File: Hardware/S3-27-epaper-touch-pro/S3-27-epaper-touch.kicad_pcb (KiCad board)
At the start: 2 copper layers, 65.4 x 71 mm, 102 parts, among them J1 AFC24-S24FIC-00, J10 Conn_01x06_Pin, J2 Conn_01x06, J3 Conn_01x06, J4 Conn_01x06_Female, J5 Groove sensor, J6 Conn_01x05_Pin, J7 Conn_01x04_Pin, J8 Conn_01x06, Q1 Si1308, Q2 Si2301, SW1 SW_Push, SW2 SW_Push, SW3 SW_Push, SW4 SW_Push, SW5 SW_Push, SW6 SW_Push, SW7 SW_Push, SW8 SW_Push, SW9 SW_Push, U1 ESP32-S3-WROOM-1-N8, U2 RT9013, U3 KoreanHropartsElecTYPE-C-31-M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, U5 BME680, U6 TPL5110, U7 RFM95W-868S2, U8 LSM6DSL

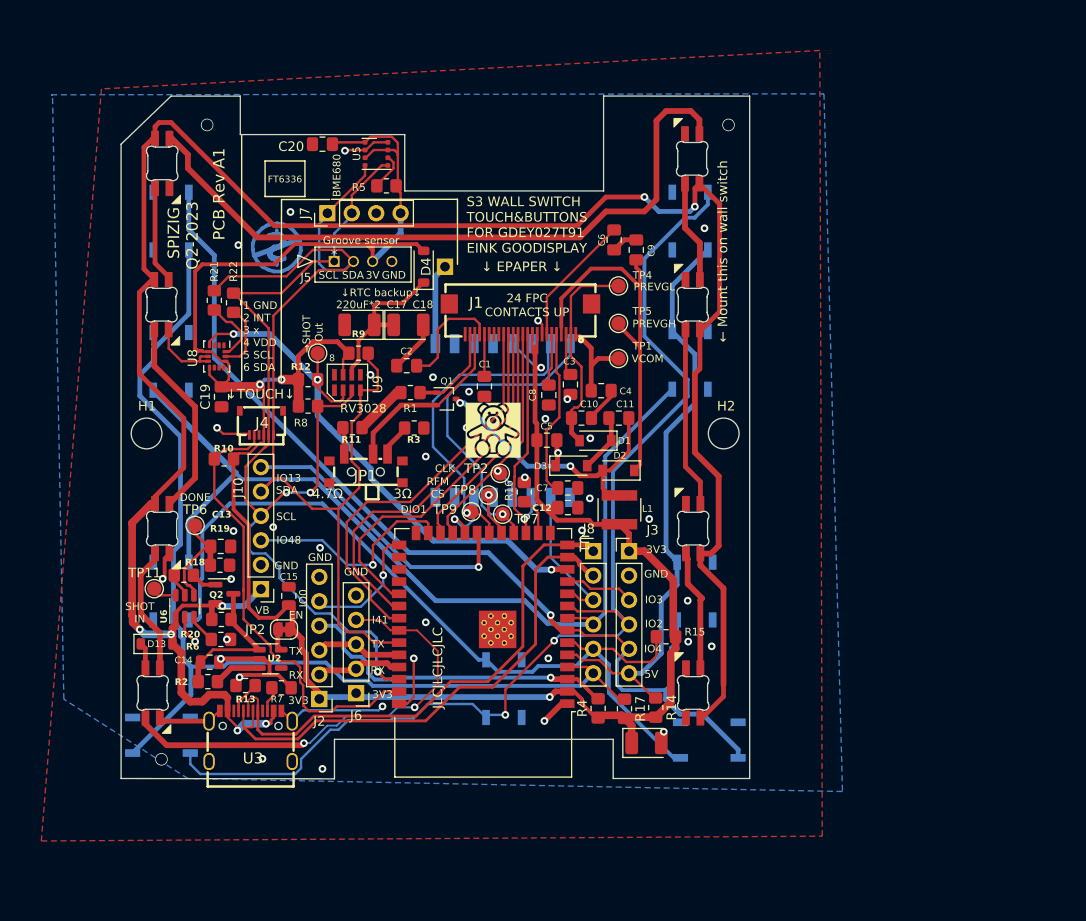
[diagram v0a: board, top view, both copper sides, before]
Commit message: Changed Footprint of BME680 and Silkscreen
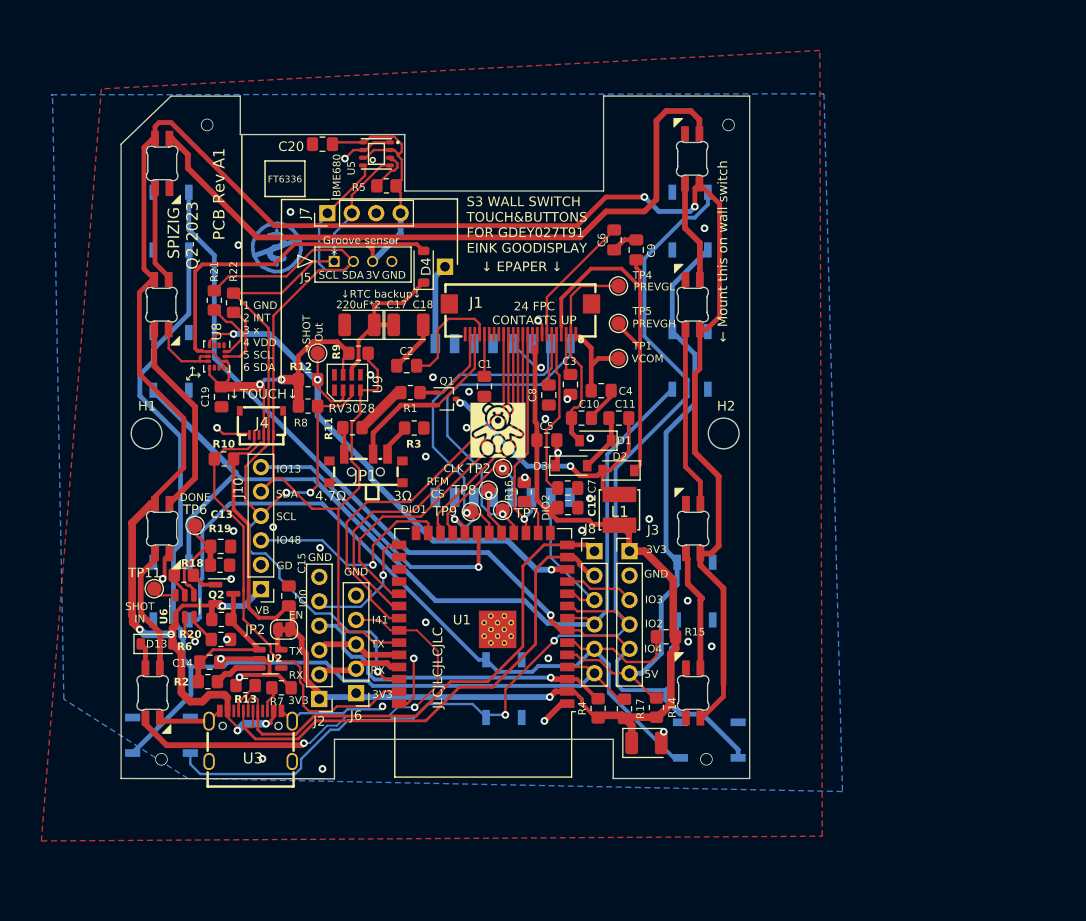
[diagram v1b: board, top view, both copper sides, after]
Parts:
- C14, C15: footprint Capacitor_SMD:C_0805_2012Metric -> Capacitor_SMD:C_0805_2012Metric_Pad1.18x1.45mm_HandSolder
- J4: value Conn_01x06_Female -> TochConn
- L1: footprint footprint:SWPA4030S1R0NT -> tp4056:IND-SMD_L4.0-W4.0
- R10, R14, R15, R17, R8, R9: value 4.7K -> 10k
- R16: value 0R -> N.C.
- R2: value 5k11 -> 10k
- R5: value 4.7K -> 10K
- U5: footprint Package_LGA:Bosch_LGA-8_3x3mm_P0.8mm_ClockwisePinNumbering -> tp4056:LGA-8_L3.0-W3.0-P0.80-TR
- moved H4 2.85 mm to (142.0, 105.0)
- moved TP2 0.56 mm to (144.5, 93.8)
- moved H3 0.50 mm to (144.0, 89.8)
- moved TP8 0.50 mm to (143.0, 96.0)
- moved TP7 0.40 mm to (144.5, 98.1)
- moved J8 0.12 mm to (154.1, 102.3)
- moved R14 0.07 mm to (160.5, 118.6)
- turned U5 to 0 degrees
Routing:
- net +3V3: track 233.0 -> 233.9 mm
- net Net-(U5-SDI): track 3.97 -> 4.67 mm
- net (no net): vias 3 -> 4
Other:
- board text added: "DIO2"
- board text added: "E-Paper&LoRa Pins: ■ EPD CS GPIO47 ■ EPD CLK GPIO21 ■ EPD BSY GPIO40 ■ EPD RST GPIO39 ■ EPD DC GPIO38 ■ EPD MOSI GPIO09"
- board text added: "GD"
- board text added: "↓"
- board text added: "■ I²C SDA IO42 ■ I²C SCL IO02 ■ TCH INT IO01 ■ SK6812 IO41 ■ Relay ON IO48 ■ Relay OFF IO13"
- board text removed: "8"
- board text removed: "E-Paper&Lora Pins: ■ EPD CS GPIO47 ■ EPD CLK GPIO21 ■ EPD BUSY GPIO40 ■ EPD RST GPIO39 ■ EPD DC GPIO38 ■ EPD MOSI GPIO09"
- board text removed: "■ I²C SDA GPIO47 ■ I²C SCL GPIO40 ■ TCH INT GPIO39 ■ SK6812 GPIO38 ■ Relay ON 48 ■ Relay OFF 13"

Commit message: Found a wiring Bug on the BME680
SDA had no pinning
wired several other lines with bigger lines
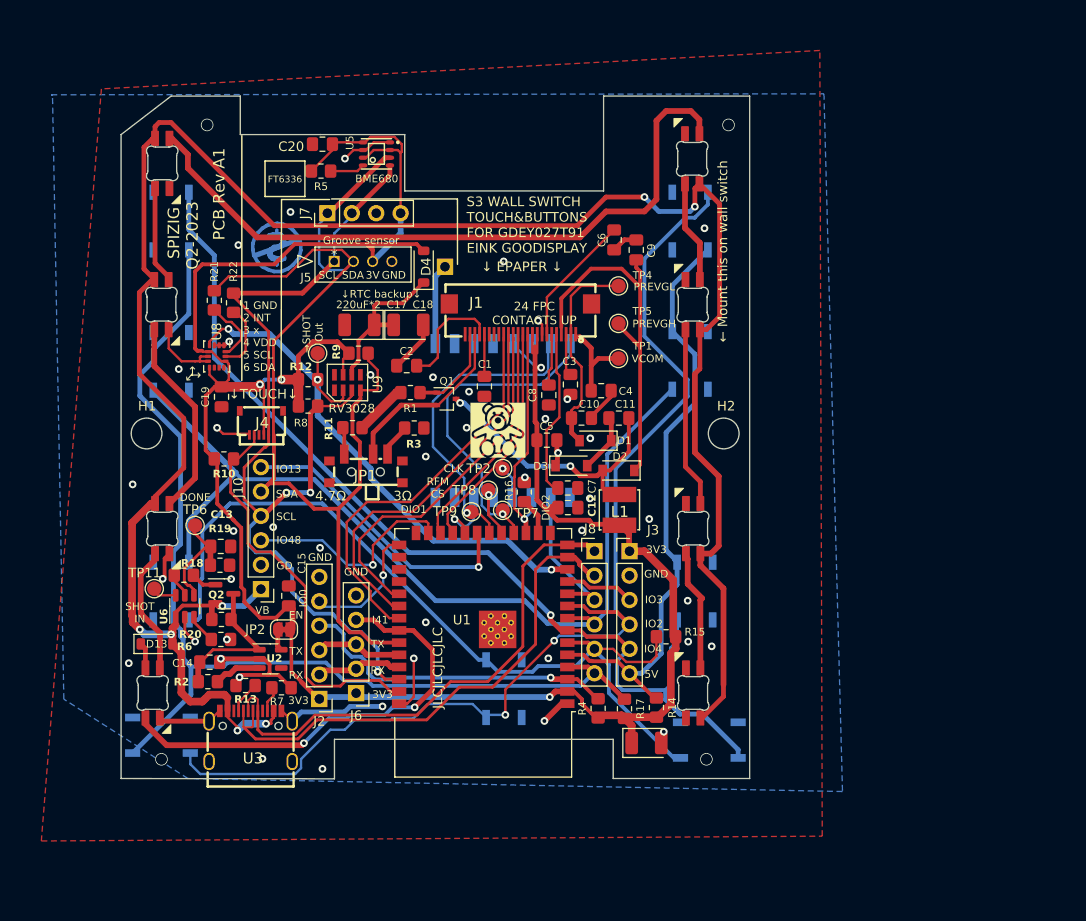
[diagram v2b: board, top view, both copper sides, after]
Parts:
- R10, R14, R15, R17, R2, R8, R9: value 10k -> 10K
- R12, R18, R19, R4, R6: value 10 K -> 10K
- R20: value 10 K -> N.C.
- moved R5 6.98 mm to (125.6, 62.8), turned to 180 degrees
- turned R10 to 0 degrees
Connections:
- R5 pad 1: Net-(U5-SDI) -> Net-(U5-SDO)
- U5 pad 3: Net-(U5-SDI) -> /TOUCH_SDA
- U5 pad 5: /TOUCH_SDA -> Net-(U5-SDO)
- U8 pad 1: unconnected-(U8-SDO/SA0-Pad1) -> GND
- U8 pad 2: unconnected-(U8-SDX-Pad2) -> GND
- U8 pad 3: unconnected-(U8-SCX-Pad3) -> GND
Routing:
- net +3V3: track 233.9 -> 242.3 mm
- net /ROW1: track 103.7 -> 111.0 mm
- net /TOUCH_SDA: track 111.7 -> 118.1 mm
- net /TOUCH_INT: track 47.5 -> 41.4 mm
- net Net-(U5-SDI): track 4.67 -> 0.00 mm
- net Net-(U5-SDO): track 0.00 -> 3.61 mm
- net /IO_15: track 98.7 -> 101.8 mm
- net GND: track 83.6 -> 85.8 mm, vias 39 -> 44
- net /IO_16: track 117.8 -> 119.6 mm
- net /EPD_MOSI: track 24.3 -> 25.9 mm
- net /IO_18: track 7.34 -> 8.75 mm
- net /SK6812_DATA: track 47.9 -> 47.2 mm
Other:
- outline, holes or cut-outs redrawn
- board text added: "@USPIZIG Q2/2023"
- board text removed: "@SPIZIG Q2/2023"

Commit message: Add files via upload
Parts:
- added R23: LDR03, OptoDevice:R_LDR_10x8.5mm_P7.6mm_Vertical, B.Cu at (168.4, 96.6)
- added R24: N.C., Resistor_SMD:R_0805_2012Metric_Pad1.20x1.40mm_HandSolder, F.Cu at (160.6, 106.8)
- C1, C2, C3, C7: value 4.7uF -> 1uF
- C10: value 4.7uF -> 4.7uF 50V_US
- C12, C9: value 4.7uF -> 4.7uF 50V US
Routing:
- net /IO_18: track 8.75 -> 23.9 mm
- net GND: track 85.8 -> 99.4 mm, vias 44 -> 45
- net /3231_INT: track 60.8 -> 64.1 mm
- net VBUS: track 224.7 -> 226.4 mm
- net /TOUCH_INT: track 41.4 -> 42.4 mm
- net /COL2: track 62.2 -> 61.7 mm

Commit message: Add files via upload
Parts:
- removed R20: N.C., Resistor_SMD:R_0805_2012Metric_Pad1.20x1.40mm_HandSolder
- added JP3: Jumper_2_Bridged, Jumper:SolderJumper-2_P1.3mm_Bridged_RoundedPad1.0x1.5mm, B.Cu at (119.4, 79.6)
- added JP4: Jumper_2_Open, Jumper:SolderJumper-2_P1.3mm_Open_RoundedPad1.0x1.5mm, F.Cu at (118.3, 110.5)
- added JP5: Jumper_2_Bridged, Jumper:SolderJumper-2_P1.3mm_Bridged_RoundedPad1.0x1.5mm, F.Cu at (124.5, 86.8)
- added TP12: VCOM, TestPoint:TestPoint_Pad_D1.5mm, F.Cu at (115.0, 85.2)
- added TP13: VCOM, TestPoint:TestPoint_Pad_D1.5mm, B.Cu at (116.2, 79.0)
- C11: value 4.7uF 50V -> 4.7uF 50V_US
- moved C19 1.83 mm to (114.6, 88.0), turned to 180 degrees
- moved R8 1.75 mm to (124.2, 89.0)
- moved R21 0.50 mm to (114.0, 76.2)
- moved R22 0.39 mm to (116.2, 76.2)
- moved R6 0.39 mm to (114.8, 111.5)
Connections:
- U8 pad 4: /3231_INT -> Net-(JP3-A)
- U8 pad 9: unconnected-(U8-INT2-Pad9) -> Net-(U8-INT2)
- U9 pad 2: /3231_INT -> Net-(JP5-B)
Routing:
- net /3231_INT: track 64.1 -> 51.2 mm, vias 3 -> 2
- net Net-(JP3-A): track 0.00 -> 8.19 mm, vias 0 -> 1
- net +3V3: track 242.5 -> 248.0 mm
- net Net-(JP5-B): track 0.00 -> 3.69 mm
- net Net-(U8-INT2): track 0.00 -> 2.16 mm
- net VBUS: track 226.4 -> 228.1 mm
- net /TOUCH_SCL: track 98.5 -> 97.5 mm
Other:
- board text added: "↓TOUCH"
- board text removed: "↓TOUCH↓"

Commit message: Add files via upload
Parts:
- added H6: MountingSwitch, MountingHole:MountingHole_3.2mm_M3, F.Cu at (137.4, 90.1)
- added R20: 100R, Resistor_SMD:R_0805_2012Metric_Pad1.20x1.40mm_HandSolder, F.Cu at (133.2, 76.2)
- added TP14: RESET_TOUCH, TestPoint:TestPoint_Pad_D1.5mm, F.Cu at (116.2, 95.4)
- moved R3 3.06 mm to (132.6, 88.1), turned to 90 degrees
- moved H3 2.25 mm to (141.8, 90.2)
- moved Q1 1.85 mm to (138.6, 84.7)
- moved R1 0.72 mm to (134.6, 85.2)
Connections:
- C17 pad 1: Net-(D4-K) -> Net-(U9-V_BCU)
- C18 pad 1: Net-(D4-K) -> Net-(U9-V_BCU)
- J4 pad 3: unconnected-(J4-Pin_3-Pad3) -> Net-(J4-Pin_3)
- U9 pad 6: Net-(D4-K) -> Net-(U9-V_BCU)
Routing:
- net Net-(D4-K): track 16.3 -> 2.83 mm
- net Net-(U9-V_BCU): track 0.00 -> 10.7 mm
- net Net-(J4-Pin_3): track 0.00 -> 6.37 mm
- net Net-(D2-A): track 28.7 -> 30.5 mm
- net Net-(Q1-G): track 9.69 -> 8.29 mm
- net GND: track 99.4 -> 100.6 mm, vias 45 -> 51
- net /TOUCH_INT: track 42.4 -> 43.5 mm
- net /DIO1: track 33.1 -> 32.0 mm
- net /EPD_BUSY: track 41.4 -> 42.2 mm
- net /EPD_RST: track 39.5 -> 40.1 mm
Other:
- board text added: "1 GND 2 INT 3 RES 4 VDD 5 SCL 6 SDA"
- board text added: "Testpoints: TP1 EPD VCOM TP2 EPD CLK TP3 INT RV3028 TP4 EPD PREVGL TP5 EPD PREVGH TP6 TPL DNE TP7 RFM D2 TP8 RFM CS TP9 RFM D1 TP10 RFM ANT TP11 TPL SHOT TP12 GYRO INT2 TP13 GYRO INT1 TP14 TOUCH RES"
- board text added: "↓RTC↓ Backup"
- board text added: "■ LORA MISO IO17 ■ LORA CS GPIO11 ■ LORA D1 GPIO12 ■ LORA D2 GPIO10"
- board text removed: "1 GND 2 INT 3 x 4 VDD 5 SCL 6 SDA"
- board text removed: "220uF*2"
- board text removed: "LORA RFM95 ■ LORA MISO IO17 ■ LORA CS GPIO11 ■ LORA D1 GPIO12 ■ LORA D2 GPIO10"
- board text removed: "↓RTC backup↓"

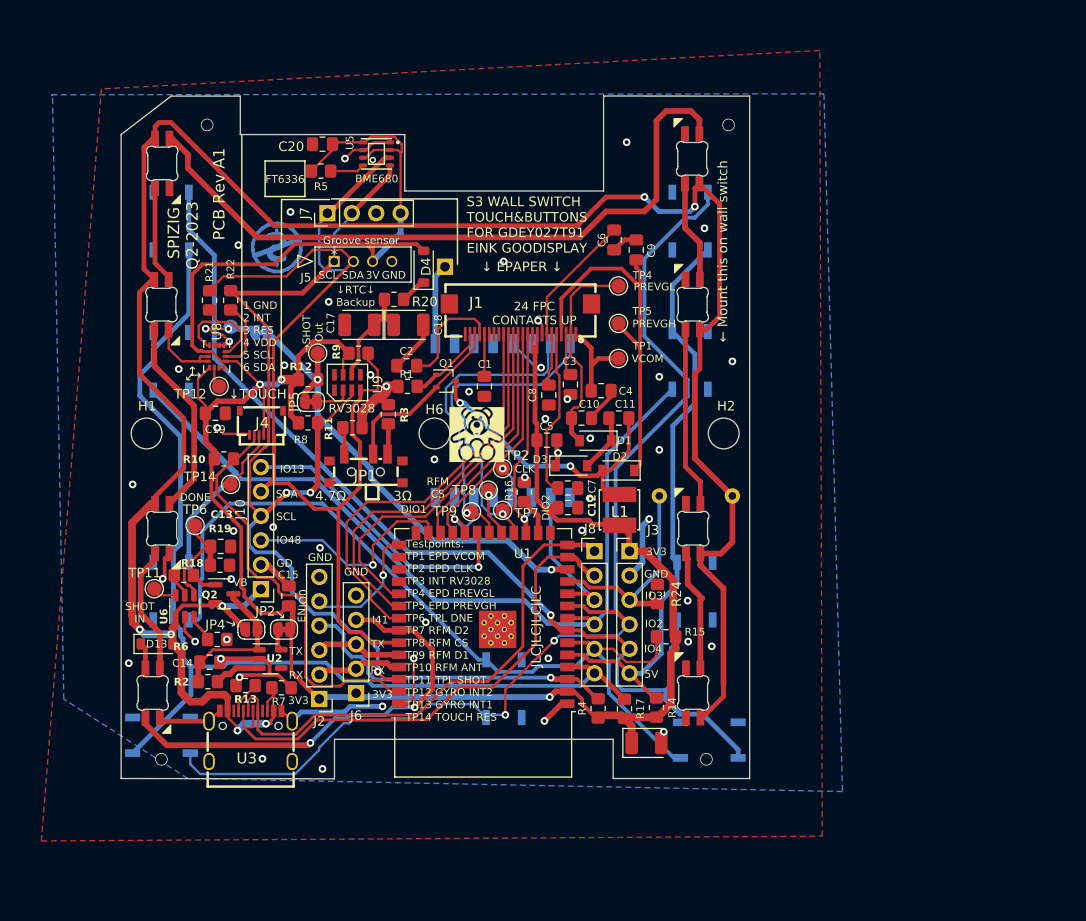
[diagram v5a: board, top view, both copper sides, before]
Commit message: Bugfixes for Production
Added a Pin Connector for a Microphone 
Fixed Bug on RV3032/RV3028 for unintended wakeup
Removed Groove Connector due to collission with Touch Controller
Changed Position of BME680
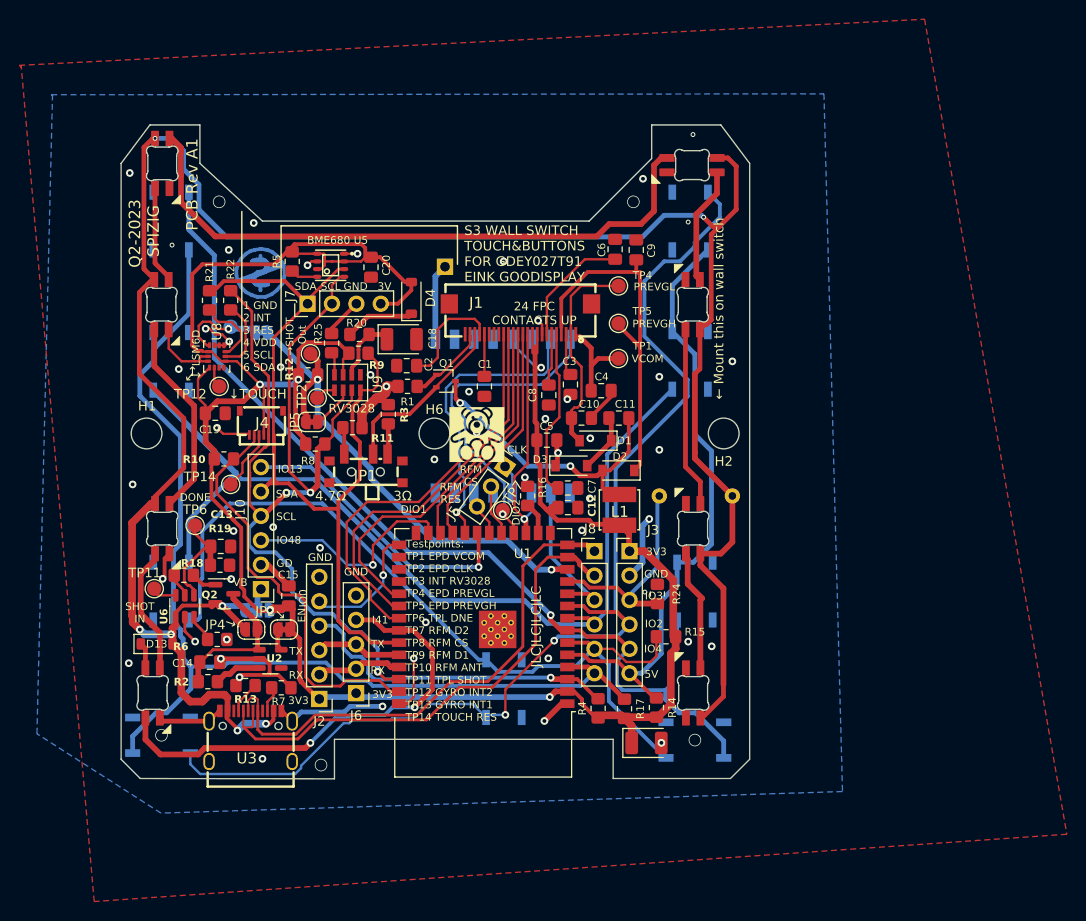
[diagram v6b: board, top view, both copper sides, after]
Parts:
- removed C17: 220uF, Capacitor_Tantalum_SMD:CP_EIA-3528-21_Kemet-B
- removed TP8, TP9: VCOM, TestPoint:TestPoint_Pad_D1.5mm
- added JP6: Jumper_3_Bridged12, Jumper:SolderJumper-3_P1.3mm_Bridged12_RoundedPad1.0x1.5mm_NumberLabels, B.Cu at (119.0, 108.5)
- added R25: 10K, Resistor_SMD:R_0805_2012Metric_Pad1.20x1.40mm_HandSolder, F.Cu at (126.7, 80.7)
- C12, C9: value 4.7uF 50V US -> 4.7uF 50V_US
- J5: value Groove sensor -> Conn_01x03_Pin; footprint footprint:MOLEX-I2C-532530470 -> Connector_PinHeader_2.54mm:PinHeader_1x03_P2.54mm_Vertical
- TP2: value VCOM -> CLKOUT
- moved J5 27.8 mm to (144.7, 93.5), turned to -35 degrees
- moved TP2 20.7 mm to (125.2, 86.4)
- moved C20 13.8 mm to (130.8, 72.8), turned to 90 degrees
- moved U5 12.5 mm to (126.6, 72.6)
- moved R5 9.87 mm to (122.6, 72.2), turned to 90 degrees
- moved J7 9.64 mm to (124.2, 76.6)
- moved D10 6.75 mm to (164.2, 57.1), turned to 180 degrees
- moved R20 5.13 mm to (129.6, 79.8), turned to 0 degrees
- moved D4 3.49 mm to (135.0, 76.0)
- moved H5 3.15 mm to (119.3, 73.4)
- moved R8 2.32 mm to (125.0, 91.2)
- moved JP5 2.10 mm to (124.7, 88.9)
- moved C18 1.66 mm to (134.0, 80.3)
- moved SW7 1.50 mm to (164.5, 122.0)
- moved C6 0.98 mm to (156.2, 70.9), turned to -90 degrees
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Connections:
- J10 pad 1: VBUS -> Net-(J10-Pin_1)
- J5 pad 1: /TOUCH_SCL -> /EPD_CLK
- J5 pad 2: /TOUCH_SDA -> /RFM_CS
- J5 pad 3: +3V3 -> /RFM_RES
- TP2 pad 1: /EPD_CLK -> Net-(U9-CLK)
- U1 pad 20: /DIO1 -> /RFM_RES
- U1 pad 22: /RFM_RES -> /DIO1
- U9 pad 1: unconnected-(U9-CLK-Pad1) -> Net-(U9-CLK)
- U9 pad 8: unconnected-(U9-EVI-Pad8) -> Net-(U9-EVI)
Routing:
- net /TOUCH_SDA: track 118.5 -> 93.6 mm
- net +3V3: track 248.2 -> 234.7 mm, vias 4 -> 5
- net Net-(D10-DIN): track 72.3 -> 65.5 mm
- net GND: track 100.6 -> 94.2 mm, vias 51 -> 53
- net Net-(D4-K): track 2.83 -> 7.29 mm
- net /RFM_RES: track 7.05 -> 3.09 mm, vias 1 -> 0
- net Net-(U9-V_BCU): track 10.7 -> 7.02 mm
- net Net-(U9-EVI): track 0.00 -> 2.42 mm
- net Net-(J10-Pin_1): track 0.00 -> 2.34 mm
- net Net-(U9-CLK): track 0.00 -> 2.13 mm
- net /COL2: track 61.7 -> 63.7 mm
- net VBUS: track 228.1 -> 230.2 mm
- net /3231_INT: track 51.2 -> 53.1 mm
- net /SK6812_DATA: track 47.2 -> 48.9 mm
- net Net-(D10-DOUT): track 10.6 -> 12.2 mm
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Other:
- board size 65.4 x 71 mm -> 65.4 x 68 mm
- board text added: "E-INK Pins: ■ EPD CS GPIO47 ■ EPD CLK GPIO21 ■ EPD BSY GPIO40 ■ EPD RST GPIO39 ■ EPD DC GPIO38 ■ EPD MOSI GPIO09"
- board text added: "I0"
- board text added: "LSM6D"
- board text added: "Q2-2023 SPIZIG"
- board text added: "R:3Ω GDEY027T9 R:4.7Ω GDEW027W3"
- board text added: "RFM RES"
- board text added: "■ I²C SDA IO42 ■ I²C SCL IO02 ■ TCH INT IO01 ■ SK6812 IO41 ■ Relay ON IO48 ■ Relay OFF IO13 ■ LDR SENS IO18"
- board text removed: "E-Paper&LoRa Pins: ■ EPD CS GPIO47 ■ EPD CLK GPIO21 ■ EPD BSY GPIO40 ■ EPD RST GPIO39 ■ EPD DC GPIO38 ■ EPD MOSI GPIO09"
- board text removed: "FT6336"
- board text removed: "R:3Ω GDEY027T91 R:4.7Ω GDEW027W3"
- board text removed: "SPIZIG Q2-2023"
- board text removed: "↓ EPAPER ↓"
- board text removed: "↓RTC↓ Backup"
- board text removed: "■ I²C SDA IO42 ■ I²C SCL IO02 ■ TCH INT IO01 ■ SK6812 IO41 ■ Relay ON IO48 ■ Relay OFF IO13"
